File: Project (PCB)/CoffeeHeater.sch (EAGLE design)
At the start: 9 parts, among them U1 POCKETBEAGLE, U2 0.56_HEX_BACKPACK

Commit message: Updated the library with all the devices and made progress in the schematics and the board
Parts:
- added BLUE: LED, ENGI301:LED
- added C1, C2: 10uF/16V X5R, microbuilder:CAP_CERAMIC0805-NOOUTLINE
- added C3: 0.1uF, microbuilder:CAP_CERAMIC0805-NOOUTLINE
- added C4: 10pF, microbuilder:CAP_CERAMIC0805-NOOUTLINE
- added C5, C6, C7: 22uF/10V X5R, microbuilder:CAP_CERAMIC0805-NOOUTLINE
- added C8: 1uF/10V X5R, microbuilder:CAP_CERAMIC0805-NOOUTLINE
- added L1: NRS5030T1R0NMGJ, microbuilder:INDUCTORTDK_VLC5045
- added Q1: BSS138, microbuilder:MOSFET-NWIDE
- added R10, R6, R9: 105K, microbuilder:RESISTOR0805_NOOUTLINE
- added R4: 2.2k, ENGI301:R_R0603
- added R5, R7: 1M, microbuilder:RESISTOR0805_NOOUTLINE
- added R8: 1K, microbuilder:RESISTOR0805_NOOUTLINE
- added U$2: TIP32C_TRANSISTOR, CoffeeHeater:TIP32C_TRANSISTOR
- added U$3: DIODE, CoffeeHeater:DIODE
- added U$4: HEATING_PAD, CoffeeHeater:HEATING_PAD
- added U3: TPS63060, microbuilder:VREG_TPS63060/1
- added X1: (no value), microbuilder:TERMBLOCK_1X2
- D1: value LED -> GREEN; device ENGI301:LED -> microbuilder:LED0805_NOOUTLINE
- renumbered D2 to GREEN, D3 to RED
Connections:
- new net 12V_VIN: C1.1, C2.1, R9.1, U$2.C, U3.VIN, X1.2
- new net 5.0V: C5.1, C6.1, C7.1, C8.1, D1.A, R5.2, R7.2, U1.VIN, U3.VOUT
- new net BASE: U$2.B, U$3.OUT
- new net ENABLE: R9.2, U3.EN
- new net HEAT_CONTROL: U$3.IN, U1.GPIO44
- new net N$1: U$2.E, U$4.2
- new net N$10: D1.C, R8.1
- new net N$11: Q1.D, R8.2
- new net N$6: L1.1, U3.L1
- new net N$7: L1.2, U3.L2
- new net N$8: C3.1, U3.VAUX
- new net N$9: C4.1, R5.1, R6.2, U3.FB
- new net PG: Q1.G, R7.1, U3.PG
- new net PS: R10.1, U3.PSYNC
- new net TEMP: R4.2, U$1.DQ, U1.GPIO45
- net GND: now also BLUE.C, C1.2, C2.2, C3.2, C4.2, C5.2, C6.2, C7.2, C8.2, Q1.S, R10.2, R6.1, U$1.GND, U$4.1, U3.GND, U3.PGND, X1.1; no longer D1.C
- net N$3: now also U1.AIN5(3.3V); no longer U1.AIN0(1.8V)
- net START_0: now also BLUE.A, U1.GPIO47; no longer D1.A, U1.GPIO27
- net START_1: now also U1.GPIO64; no longer U1.GPIO44
- net VDD_5V: now also R4.1, U$1.VDD
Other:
- note added: "Voltage Regulator"

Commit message: Minor updates to the general layout
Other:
- note added: "Battery Input"
- moved on the sheet: X1
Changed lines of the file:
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@@
 <plain>
 <text x="314.96" y="20.32" size="2.54" layer="94">ENGI301 - PCB Project</text>
-<text x="233.68" y="241.3" size="3.81" layer="97">Temperature Display</text>
+<text x="210.82" y="246.38" size="3.81" layer="97">Temperature Display</text>
 <wire x1="210.82" y1="185.42" x2="210.82" y2="109.22" width="0.1524" layer="97"/>
 <wire x1="297.18" y1="185.42" x2="297.18" y2="109.22" width="0.1524" layer="97"/>
@@
 <text x="66.04" y="246.38" size="3.81" layer="97">PocketBeagle</text>
 <text x="22.86" y="83.82" size="3.81" layer="97">Temperature Selector</text>
-<wire x1="137.16" y1="266.7" x2="137.16" y2="20.32" width="0.1524" layer="97"/>
+<wire x1="137.16" y1="254" x2="137.16" y2="7.62" width="0.1524" layer="97"/>
 <wire x1="142.24" y1="104.14" x2="378.46" y2="104.14" width="0.1524" layer="97"/>
 <text x="144.78" y="96.52" size="3.81" layer="97">Voltage Regulator</text>
+<wire x1="297.18" y1="251.46" x2="297.18" y2="195.58" width="0.1524" layer="97"/>
+<text x="304.8" y="246.38" size="3.81" layer="97">Battery Input</text>
 </plain>
 <instances>
@@
 <attribute name="VALUE" x="323.596" y="27.94" size="1.27" layer="96"/>
 </instance>
-<instance part="X1" gate="G$1" x="342.9" y="88.9" rot="R180">
-<attribute name="VALUE" x="345.44" y="93.98" size="1.27" layer="96" rot="R180"/>
-<attribute name="NAME" x="345.44" y="81.28" size="1.27" layer="95" rot="R180"/>
-</instance>
-<instance part="U$19" gate="G$1" x="347.98" y="81.28">
-<attribute name="VALUE" x="346.456" y="78.74" size="1.27" layer="96"/>
+<instance part="X1" gate="G$1" x="330.2" y="220.98" rot="R180">
+<attribute name="VALUE" x="332.74" y="226.06" size="1.27" layer="96" rot="R180"/>
+<attribute name="NAME" x="332.74" y="213.36" size="1.27" layer="95" rot="R180"/>
+</instance>
+<instance part="U$19" gate="G$1" x="335.28" y="213.36">
+<attribute name="VALUE" x="333.756" y="210.82" size="1.27" layer="96"/>
 </instance>
 <instance part="Q1" gate="G$1" x="322.58" y="40.64">
@@
 <segment>
 <pinref part="U$19" gate="G$1" pin="GND"/>
-<wire x1="347.98" y1="86.36" x2="347.98" y2="83.82" width="0.1524" layer="91"/>
+<wire x1="335.28" y1="218.44" x2="335.28" y2="215.9" width="0.1524" layer="91"/>
 <pinref part="X1" gate="G$1" pin="1"/>
 </segment>
@@
 <segment>
 <pinref part="X1" gate="G$1" pin="2"/>
-<wire x1="347.98" y1="88.9" x2="347.98" y2="96.52" width="0.1524" layer="91"/>
-<label x="350.52" y="91.44" size="1.778" layer="95" rot="R90"/>
-</segment>
-<segment>
+<wire x1="335.28" y1="220.98" x2="335.28" y2="228.6" width="0.1524" layer="91"/>
+<label x="337.82" y="223.52" size="1.778" layer="95" rot="R90"/>
+</segment>
+<segment>

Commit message: Started routing some of the connections
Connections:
- net GND: now also U$4.2; no longer U$4.1
- net N$1: now also U$4.1; no longer U$4.2
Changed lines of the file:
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@@
 </instance>
 <instance part="U$3" gate="G$1" x="323.215" y="144.145"/>
-<instance part="U$4" gate="G$1" x="345.44" y="121.92" rot="R90">
-<attribute name="NAME" x="342.9" y="119.38" size="1.778" layer="95" rot="R90" display="off"/>
-<attribute name="VALUE" x="342.9" y="116.84" size="1.778" layer="96" rot="R90"/>
+<instance part="U$4" gate="G$1" x="345.44" y="124.46" rot="R270">
+<attribute name="NAME" x="347.98" y="127" size="1.778" layer="95" rot="R270" display="off"/>
+<attribute name="VALUE" x="347.98" y="129.54" size="1.778" layer="96" rot="R270"/>
 </instance>
 <instance part="GND4" gate="1" x="345.44" y="109.22">
@@
 </segment>
 <segment>
-<pinref part="U$4" gate="G$1" pin="1"/>
-<pinref part="GND4" gate="1" pin="GND"/>
-<wire x1="345.44" y1="116.84" x2="345.44" y2="111.76" width="0.1524" layer="91"/>
-</segment>
-<segment>
 <pinref part="U3" gate="G$1" pin="GND"/>
 <pinref part="U$5" gate="G$1" pin="GND"/>
@@
 <pinref part="U$28" gate="G$1" pin="GND"/>
 <wire x1="218.44" y1="25.4" x2="218.44" y2="30.48" width="0.1524" layer="91"/>
+</segment>
+<segment>
+<pinref part="U$4" gate="G$1" pin="2"/>
+<pinref part="GND4" gate="1" pin="GND"/>
+<wire x1="345.44" y1="119.38" x2="345.44" y2="111.76" width="0.1524" layer="91"/>
 </segment>
 </net>
@@
 <wire x1="104.14" y1="157.48" x2="121.92" y2="157.48" width="0.1524" layer="91"/>
 <label x="114.3" y="157.48" size="1.778" layer="95"/>
-</segment>
-</net>
-<net name="N$1" class="0">
-<segment>
-<pinref part="U$2" gate="G$1" pin="E"/>
-<pinref part="U$4" gate="G$1" pin="2"/>
-<wire x1="345.44" y1="133.985" x2="345.44" y2="127" width="0.1524" layer="91"/>
 </segment>
 </net>
@@
 </segment>
 </net>
+<net name="N$1" class="0">
+<segment>
+<pinref part="U$2" gate="G$1" pin="E"/>
+<pinref part="U$4" gate="G$1" pin="1"/>
+<wire x1="345.44" y1="133.985" x2="345.44" y2="129.54" width="0.1524" layer="91"/>
+</segment>
+</net>

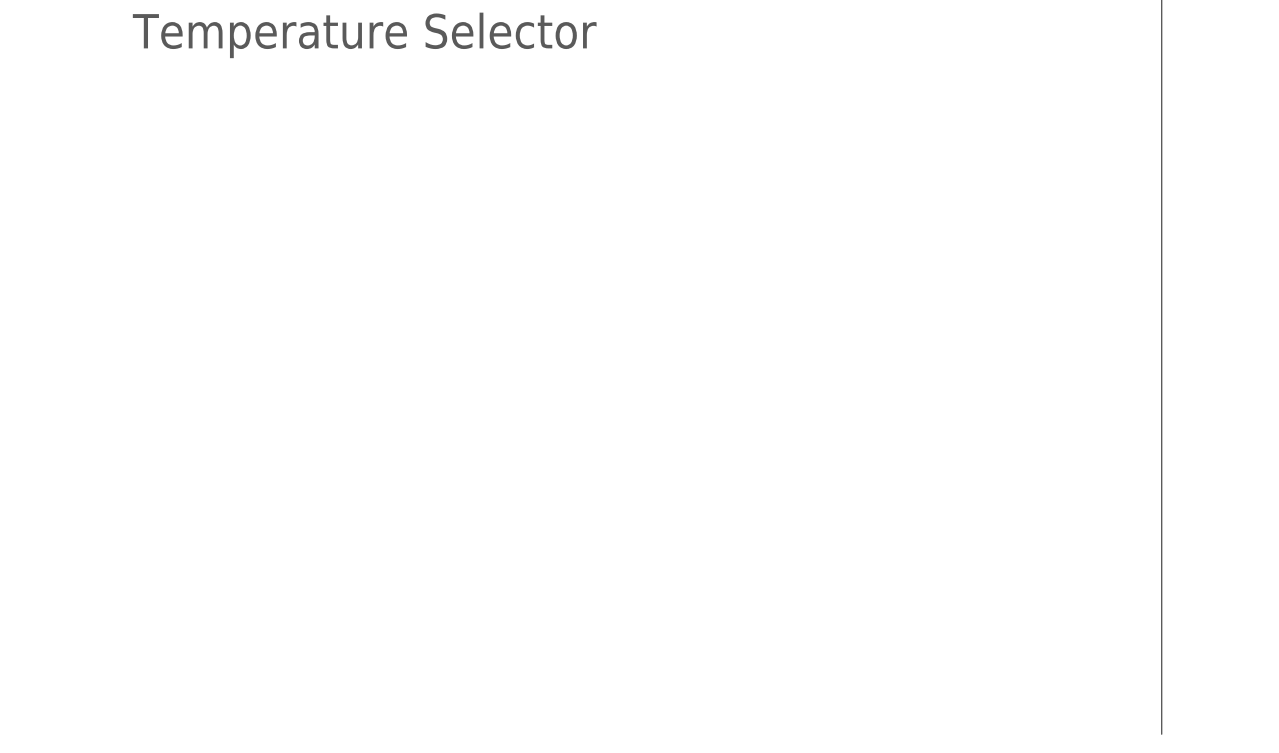
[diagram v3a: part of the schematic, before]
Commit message: Added mechanical parts and updated routes.
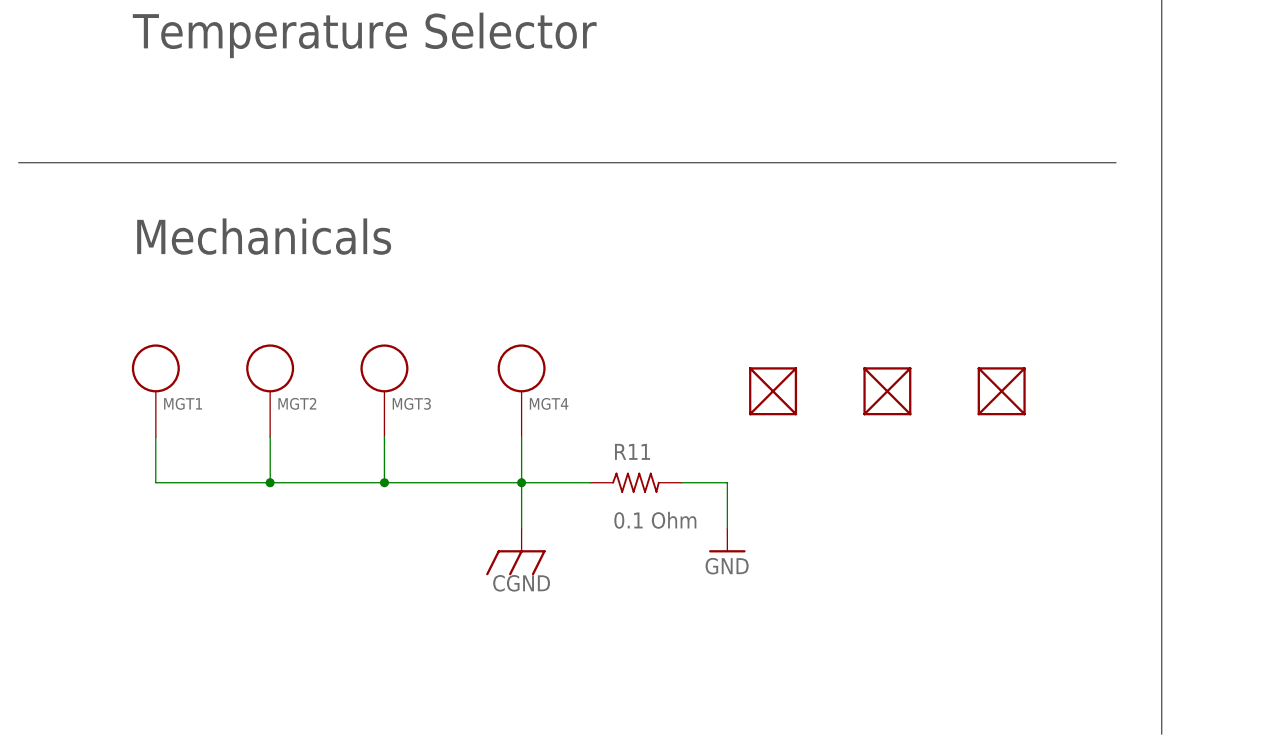
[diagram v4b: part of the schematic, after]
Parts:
- added FUD1, FUD2, FUD3: FIDUCIAL, Whac-a-mole:FIDUCIAL
- added MGT1, MGT2, MGT3, MGT4: MOUNTING_HOLE, Whac-a-mole:MOUNTING_HOLE
- added R11: 0.1 Ohm, Whac-a-mole:R_R0805
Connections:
- new net CGND: MGT1.P$1, MGT2.P$1, MGT3.P$1, MGT4.P$1, R11.1
- net GND: now also R11.2
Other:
- note added: "Mechanicals"
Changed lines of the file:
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@@
 <part name="R10" library="microbuilder" deviceset="RESISTOR" device="0805_NOOUTLINE" value="105K"/>
 <part name="U$28" library="microbuilder" deviceset="GND" device=""/>
+<part name="MGT1" library="Whac-a-mole" deviceset="MOUNTING_HOLE" device=""/>
+<part name="MGT2" library="Whac-a-mole" deviceset="MOUNTING_HOLE" device=""/>
+<part name="MGT3" library="Whac-a-mole" deviceset="MOUNTING_HOLE" device=""/>
+<part name="MGT4" library="Whac-a-mole" deviceset="MOUNTING_HOLE" device=""/>
+<part name="FUD1" library="Whac-a-mole" deviceset="FIDUCIAL" device=""/>
+<part name="FUD2" library="Whac-a-mole" deviceset="FIDUCIAL" device=""/>
+<part name="FUD3" library="Whac-a-mole" deviceset="FIDUCIAL" device=""/>
+<part name="SUPPLY12" library="Whac-a-mole" deviceset="CGND" device=""/>
+<part name="R11" library="Whac-a-mole" deviceset="R_" device="R0805" value="0.1 Ohm"/>
+<part name="GND14" library="Whac-a-mole" deviceset="GND" device=""/>
 </parts>
 <sheets>
@@
 <wire x1="297.18" y1="251.46" x2="297.18" y2="195.58" width="0.1524" layer="97"/>
 <text x="304.8" y="246.38" size="3.81" layer="97">Battery Input</text>
+<wire x1="10.16" y1="71.12" x2="132.08" y2="71.12" width="0.1524" layer="97"/>
+<text x="22.86" y="60.96" size="3.81" layer="97">Mechanicals</text>
 </plain>
 <instances>
@@
 <instance part="U$28" gate="G$1" x="218.44" y="22.86">
 <attribute name="VALUE" x="216.916" y="20.32" size="1.27" layer="96"/>
+</instance>
+<instance part="MGT1" gate="G$1" x="25.4" y="45.72">
+<attribute name="NAME" x="26.162" y="43.688" size="1.27" layer="95"/>
+</instance>
+<instance part="MGT2" gate="G$1" x="38.1" y="45.72">
+<attribute name="NAME" x="38.862" y="43.688" size="1.27" layer="95"/>
+</instance>
+<instance part="MGT3" gate="G$1" x="50.8" y="45.72">
+<attribute name="NAME" x="51.562" y="43.688" size="1.27" layer="95"/>
+</instance>
+<instance part="MGT4" gate="G$1" x="66.04" y="45.72">
+<attribute name="NAME" x="66.802" y="43.688" size="1.27" layer="95"/>
+</instance>
+<instance part="FUD1" gate="G$1" x="93.98" y="45.72"/>
+<instance part="FUD2" gate="G$1" x="106.68" y="45.72"/>
+<instance part="FUD3" gate="G$1" x="119.38" y="45.72"/>
+<instance part="SUPPLY12" gate="G$1" x="66.04" y="27.94">
+<attribute name="VALUE" x="66.04" y="24.384" size="1.778" layer="96" align="center"/>
+</instance>
+<instance part="R11" gate="G$1" x="78.74" y="35.56">
+<attribute name="NAME" x="76.2" y="38.1" size="1.778" layer="95"/>
+<attribute name="VALUE" x="76.2" y="30.48" size="1.778" layer="96"/>
+</instance>
+<instance part="GND14" gate="1" x="88.9" y="27.94">
+<attribute name="VALUE" x="86.36" y="25.4" size="1.778" layer="96"/>
 </instance>
 </instances>
@@
 <pinref part="GND4" gate="1" pin="GND"/>
 <wire x1="345.44" y1="119.38" x2="345.44" y2="111.76" width="0.1524" layer="91"/>
+</segment>
+<segment>
+<pinref part="R11" gate="G$1" pin="2"/>
+<wire x1="83.82" y1="35.56" x2="88.9" y2="35.56" width="0.1524" layer="91"/>
+<pinref part="GND14" gate="1" pin="GND"/>
+<wire x1="88.9" y1="35.56" x2="88.9" y2="30.48" width="0.1524" layer="91"/>
 </segment>
 </net>
@@
 </segment>
 </net>
+<net name="CGND" class="0">
+<segment>
+<pinref part="SUPPLY12" gate="G$1" pin="CGND"/>
+<pinref part="MGT4" gate="G$1" pin="P$1"/>
+<pinref part="MGT1" gate="G$1" pin="P$1"/>
+<wire x1="66.04" y1="35.56" x2="66.04" y2="40.64" width="0.1524" layer="91"/>
+<wire x1="25.4" y1="40.64" x2="25.4" y2="35.56" width="0.1524" layer="91"/>
+<pinref part="R11" gate="G$1" pin="1"/>
+<wire x1="25.4" y1="35.56" x2="38.1" y2="35.56" width="0.1524" layer="91"/>
+<wire x1="38.1" y1="35.56" x2="50.8" y2="35.56" width="0.1524" layer="91"/>
+<wire x1="50.8" y1="35.56" x2="66.04" y2="35.56" width="0.1524" layer="91"/>
+<wire x1="66.04" y1="35.56" x2="73.66" y2="35.56" width="0.1524" layer="91"/>
+<wire x1="66.04" y1="30.48" x2="66.04" y2="35.56" width="0.1524" layer="91"/>
+<junction x="66.04" y="35.56"/>
+<pinref part="MGT3" gate="G$1" pin="P$1"/>
+<wire x1="50.8" y1="40.64" x2="50.8" y2="35.56" width="0.1524" layer="91"/>
+<junction x="50.8" y="35.56"/>
+<pinref part="MGT2" gate="G$1" pin="P$1"/>
+<wire x1="38.1" y1="40.64" x2="38.1" y2="35.56" width="0.1524" layer="91"/>
+<junction x="38.1" y="35.56"/>
+</segment>
+</net>
